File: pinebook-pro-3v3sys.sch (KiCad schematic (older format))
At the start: 19 parts, among them J1 Conn_01x03, J2 Conn_02x03_Counter_Clockwise, J3 Conn_01x01, J4 Conn_01x03, J5 Conn_01x01, U1 TPS63806

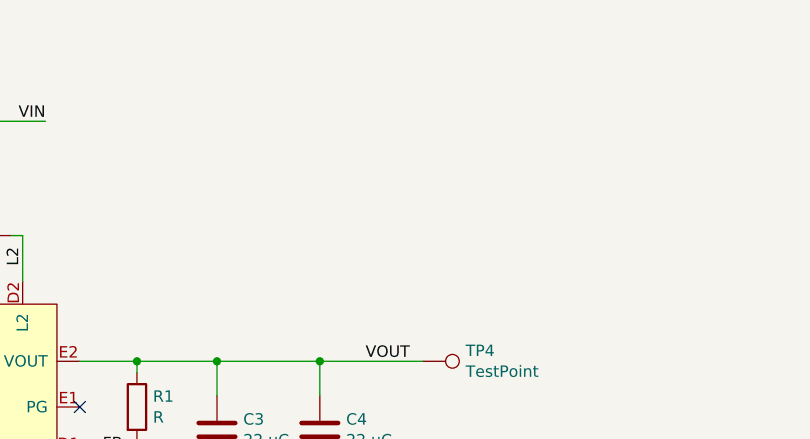
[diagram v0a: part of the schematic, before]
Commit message: Add components for mousebites
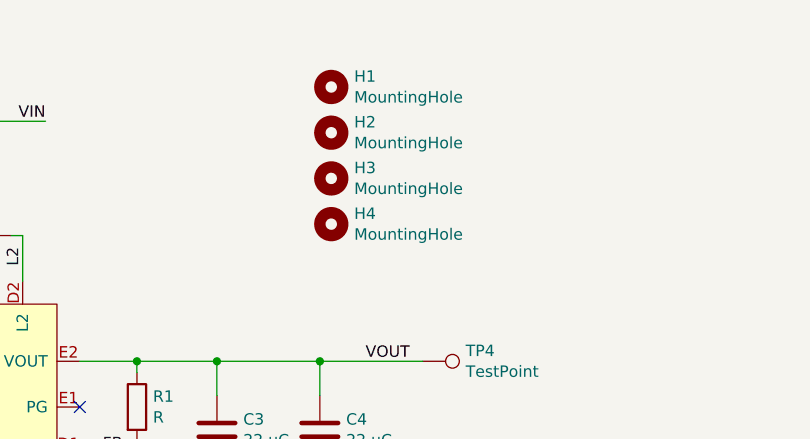
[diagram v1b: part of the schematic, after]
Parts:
- added H1, H2, H3, H4: MountingHole, Mousebite:Mousebite_0.3mm, symbol Mechanical:MountingHole
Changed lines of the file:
@@
 NoConn ~ 9150 3500
 NoConn ~ 9150 3600
+$Comp
+L Mechanical:MountingHole H1
+U 1 1 5DE0908C
+P 6500 1600
+F 0 "H1" H 6600 1646 50  0000 L CNN
+F 1 "MountingHole" H 6600 1555 50  0000 L CNN
+F 2 "Mousebite:Mousebite_0.3mm" H 6500 1600 50  0001 C CNN
+F 3 "~" H 6500 1600 50  0001 C CNN
+	1    6500 1600
+	1    0    0    -1
+$EndComp
+$Comp
+L Mechanical:MountingHole H2
+U 1 1 5DE09669
+P 6500 1800
+F 0 "H2" H 6600 1846 50  0000 L CNN
+F 1 "MountingHole" H 6600 1755 50  0000 L CNN
+F 2 "Mousebite:Mousebite_0.3mm" H 6500 1800 50  0001 C CNN
+F 3 "~" H 6500 1800 50  0001 C CNN
+	1    6500 1800
+	1    0    0    -1
+$EndComp
+$Comp
+L Mechanical:MountingHole H3
+U 1 1 5DE0A1FC
+P 6500 2000
+F 0 "H3" H 6600 2046 50  0000 L CNN
+F 1 "MountingHole" H 6600 1955 50  0000 L CNN
+F 2 "Mousebite:Mousebite_0.3mm" H 6500 2000 50  0001 C CNN
+F 3 "~" H 6500 2000 50  0001 C CNN
+	1    6500 2000
+	1    0    0    -1
+$EndComp
+$Comp
+L Mechanical:MountingHole H4
+U 1 1 5DE0AE24
+P 6500 2200
+F 0 "H4" H 6600 2246 50  0000 L CNN
+F 1 "MountingHole" H 6600 2155 50  0000 L CNN
+F 2 "Mousebite:Mousebite_0.3mm" H 6500 2200 50  0001 C CNN
+F 3 "~" H 6500 2200 50  0001 C CNN
+	1    6500 2200
+	1    0    0    -1
+$EndComp
 $EndSCHEMATC

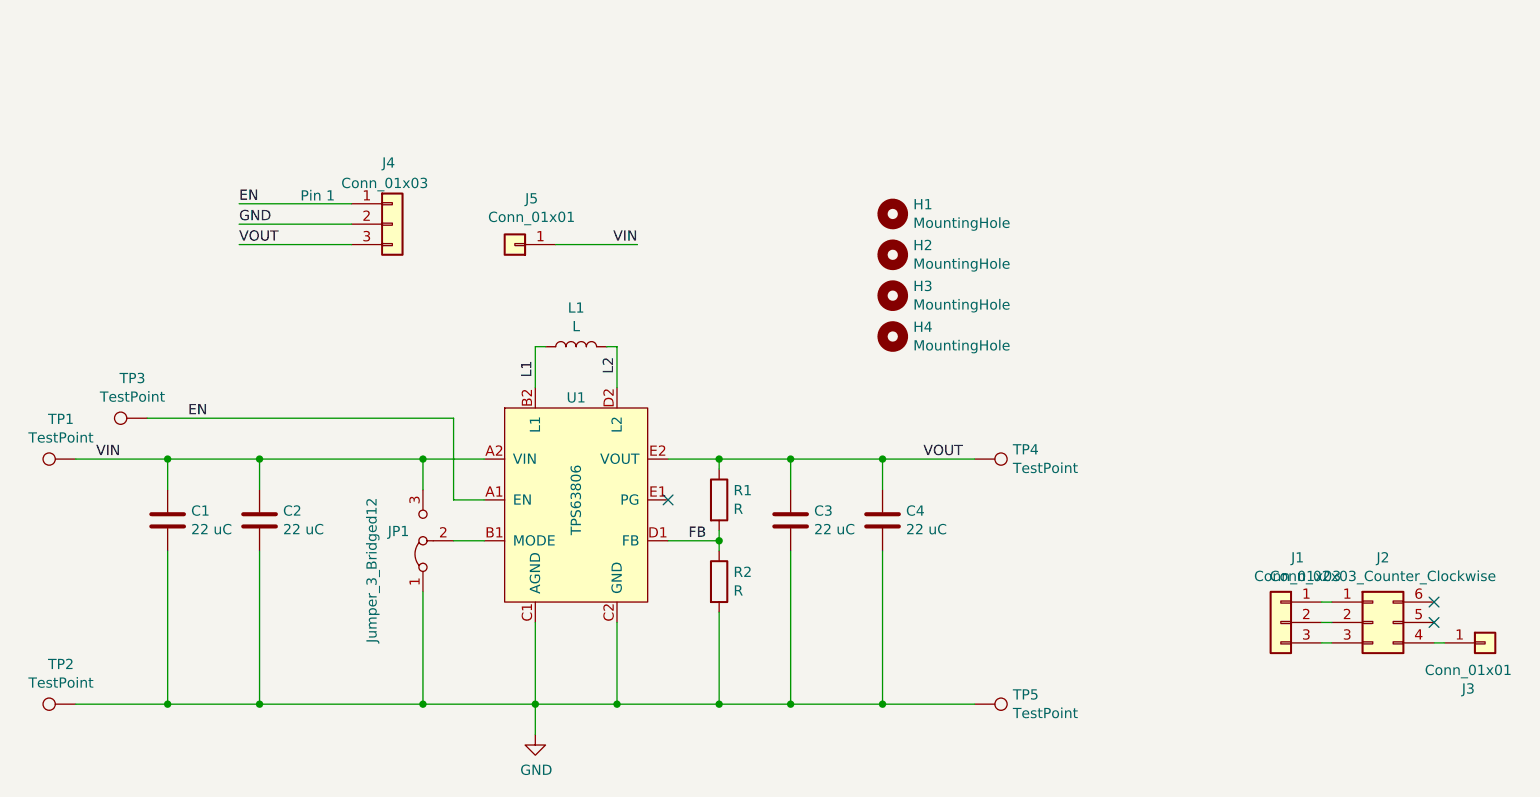
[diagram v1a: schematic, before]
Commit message: Parameterize feedback divider resistors for 3.3 V
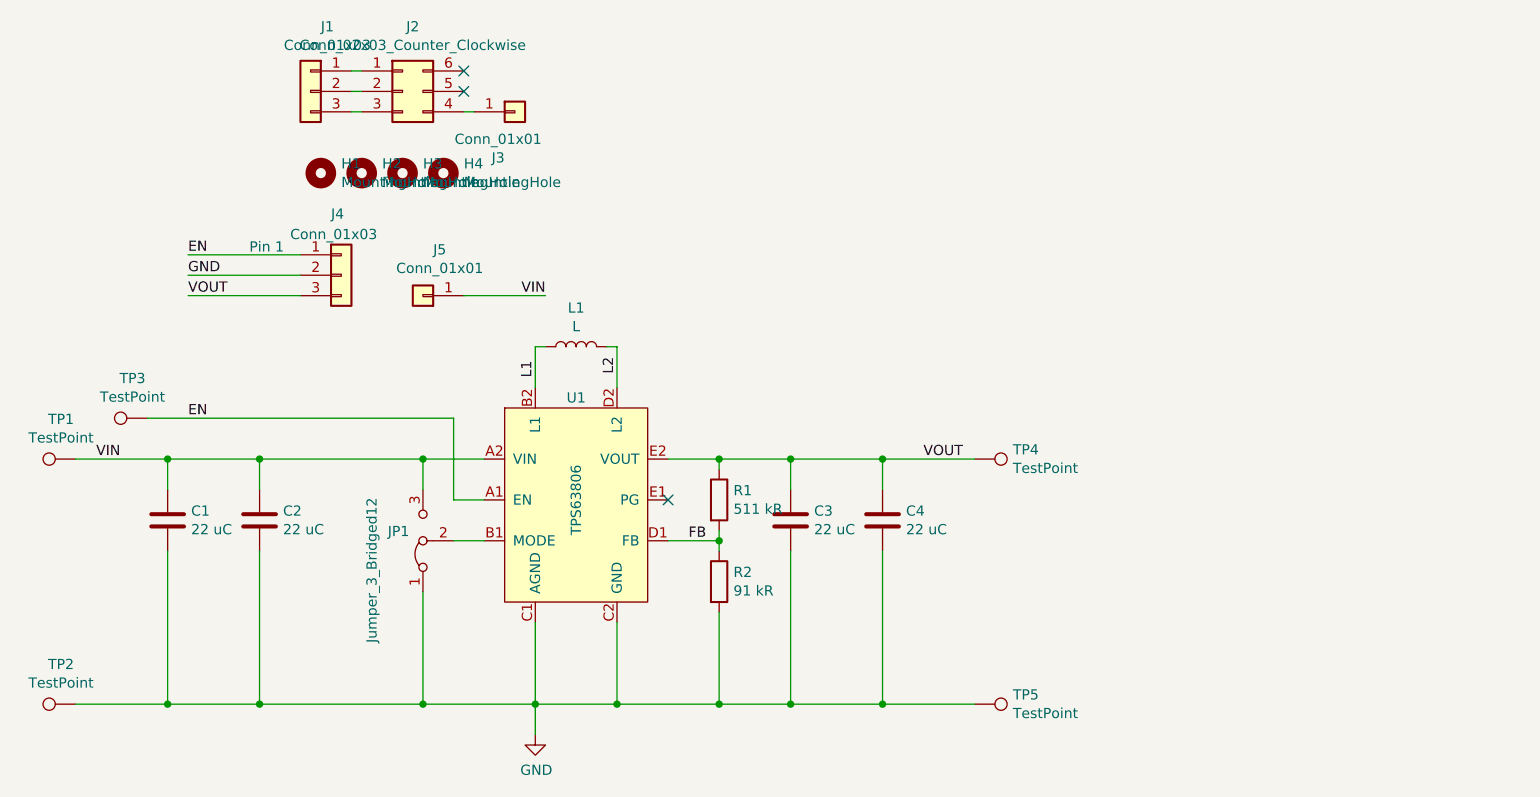
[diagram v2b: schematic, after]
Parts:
- R1: value R -> 511 kR
- R2: value R -> 91 kR
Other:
- moved on the sheet: H1, H2, H3, H4, J1, J2, J3, J4, J5
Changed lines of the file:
@@
 encoding utf-8
 Sheet 1 1
-Title ""
-Date ""
-Rev ""
-Comp ""
+Title "PInebook Pro VCC3V3_SYS regulator board"
+Date "2019-11-24"
+Rev "A"
+Comp "Tobias Schramm"
 Comment1 ""
 Comment2 ""
@@
 P 5650 3000
 F 0 "R1" H 5720 3046 50  0000 L CNN
-F 1 "R" H 5720 2955 50  0000 L CNN
+F 1 "511 kR" H 5720 2955 50  0000 L CNN
 F 2 "Resistor_SMD:R_0402_1005Metric" V 5580 3000 50  0001 C CNN
 F 3 "~" H 5650 3000 50  0001 C CNN
@@
 P 5650 3400
 F 0 "R2" H 5720 3446 50  0000 L CNN
-F 1 "R" H 5720 3355 50  0000 L CNN
+F 1 "91 kR" H 5720 3355 50  0000 L CNN
 F 2 "Resistor_SMD:R_0402_1005Metric" V 5580 3400 50  0001 C CNN
 F 3 "~" H 5650 3400 50  0001 C CNN
@@
 L Connector_Generic:Conn_02x03_Counter_Clockwise J2
 U 1 1 5DDB932F
-P 8850 3600
-F 0 "J2" H 8900 3917 50  0000 C CNN
-F 1 "Conn_02x03_Counter_Clockwise" H 8900 3826 50  0000 C CNN
-F 2 "Castellations:SOT-23-6" H 8850 3600 50  0001 C CNN
-F 3 "~" H 8850 3600 50  0001 C CNN
-	1    8850 3600
+P 4100 1000
+F 0 "J2" H 4150 1317 50  0000 C CNN
+F 1 "Conn_02x03_Counter_Clockwise" H 4150 1226 50  0000 C CNN
+F 2 "Castellations:SOT-23-6" H 4100 1000 50  0001 C CNN
+F 3 "~" H 4100 1000 50  0001 C CNN
+	1    4100 1000
 	1    0    0    -1
 $EndComp
@@
 L Connector_Generic:Conn_01x03 J1
 U 1 1 5DDBA462
-P 8400 3600
-F 0 "J1" H 8318 3917 50  0000 C CNN
-F 1 "Conn_01x03" H 8318 3826 50  0000 C CNN
-F 2 "Connector_PinHeader_0.6mm:PinHeader_1x03_P0.95mm" H 8400 3600 50  0001 C CNN
-F 3 "~" H 8400 3600 50  0001 C CNN
-	1    8400 3600
+P 3650 1000
+F 0 "J1" H 3568 1317 50  0000 C CNN
+F 1 "Conn_01x03" H 3568 1226 50  0000 C CNN
+F 2 "Connector_PinHeader_0.6mm:PinHeader_1x03_P0.95mm" H 3650 1000 50  0001 C CNN
+F 3 "~" H 3650 1000 50  0001 C CNN
+	1    3650 1000
 	-1   0    0    -1
 $EndComp
 Wire Wire Line
-	8600 3500 8650 3500
-Wire Wire Line
-	8600 3600 8650 3600
-Wire Wire Line
-	8600 3700 8650 3700
+	3850 900  3900 900
+Wire Wire Line
+	3850 1000 3900 1000
+Wire Wire Line
+	3850 1100 3900 1100
 Text Label 4750 2400 1    50   ~ 0
 L1
@@
 L Connector_Generic:Conn_01x03 J4
 U 1 1 5DDD7088
-P 4050 1650
-F 0 "J4" H 4000 1950 50  0000 L CNN
-F 1 "Conn_01x03" H 3800 1850 50  0000 L CNN
-F 2 "Connector_PinHeader_0.6mm:PinHeader_1x03_P0.95mm" H 4050 1650 50  0001 C CNN
-F 3 "~" H 4050 1650 50  0001 C CNN
-	1    4050 1650
-	1    0    0    -1
-$EndComp
-Text Notes 3600 1550 0    50   ~ 0
+P 3800 1900
+F 0 "J4" H 3750 2200 50  0000 L CNN
+F 1 "Conn_01x03" H 3550 2100 50  0000 L CNN
+F 2 "Connector_PinHeader_0.6mm:PinHeader_1x03_P0.95mm" H 3800 1900 50  0001 C CNN
+F 3 "~" H 3800 1900 50  0001 C CNN
+	1    3800 1900
+	1    0    0    -1
+$EndComp
+Text Notes 3350 1800 0    50   ~ 0
 Pin 1\n
 Wire Wire Line
-	3850 1550 3300 1550
-Text Label 3300 1550 0    50   ~ 0
+	3600 1800 3050 1800
+Text Label 3050 1800 0    50   ~ 0
 EN
 Wire Wire Line
-	3850 1650 3300 1650
-Text Label 3300 1650 0    50   ~ 0
+	3600 1900 3050 1900
+Text Label 3050 1900 0    50   ~ 0
 GND
 Wire Wire Line
-	3850 1750 3300 1750
-Text Label 3300 1750 0    50   ~ 0
+	3600 2000 3050 2000
+Text Label 3050 2000 0    50   ~ 0
 VOUT
 Wire Wire Line
-	4850 1750 5250 1750
-Text Label 5250 1750 2    50   ~ 0
+	4400 2000 4800 2000
+Text Label 4800 2000 2    50   ~ 0
 VIN
 $Comp
@@
 L Connector_Generic:Conn_01x01 J5
 U 1 1 5DDE7032
-P 4650 1750
-F 0 "J5" H 4568 1525 50  0000 C CNN
-F 1 "Conn_01x01" H 4568 1616 50  0000 C CNN
-F 2 "Connector_PinHeader_0.6mm:PinHeader_1x01_P0.95mm" H 4650 1750 50  0001 C CNN
-F 3 "~" H 4650 1750 50  0001 C CNN
-	1    4650 1750
+P 4200 2000
+F 0 "J5" H 4118 1775 50  0000 C CNN
+F 1 "Conn_01x01" H 4118 1866 50  0000 C CNN
+F 2 "Connector_PinHeader_0.6mm:PinHeader_1x01_P0.95mm" H 4200 2000 50  0001 C CNN
+F 3 "~" H 4200 2000 50  0001 C CNN
+	1    4200 2000
 	-1   0    0    1
 $EndComp
@@
 L Connector_Generic:Conn_01x01 J3
 U 1 1 5DDFD1C1
-P 9400 3700
-F 0 "J3" H 9318 3475 50  0000 C CNN
-F 1 "Conn_01x01" H 9318 3566 50  0000 C CNN
-F 2 "Connector_PinHeader_0.6mm:PinHeader_1x01_P0.95mm" H 9400 3700 50  0001 C CNN
-F 3 "~" H 9400 3700 50  0001 C CNN
-	1    9400 3700
-	1    0    0    -1
-$EndComp
-Wire Wire Line
-	9200 3700 9150 3700
-NoConn ~ 9150 3500
-NoConn ~ 9150 3600
+P 4650 1100
+F 0 "J3" H 4568 875 50  0000 C CNN
+F 1 "Conn_01x01" H 4568 966 50  0000 C CNN
+F 2 "Connector_PinHeader_0.6mm:PinHeader_1x01_P0.95mm" H 4650 1100 50  0001 C CNN
+F 3 "~" H 4650 1100 50  0001 C CNN
+	1    4650 1100
+	1    0    0    -1
+$EndComp
+Wire Wire Line
+	4450 1100 4400 1100
+NoConn ~ 4400 900
+NoConn ~ 4400 1000
 $Comp
 L Mechanical:MountingHole H1
 U 1 1 5DE0908C
-P 6500 1600
-F 0 "H1" H 6600 1646 50  0000 L CNN
-F 1 "MountingHole" H 6600 1555 50  0000 L CNN
-F 2 "Mousebite:Mousebite_0.3mm" H 6500 1600 50  0001 C CNN
-F 3 "~" H 6500 1600 50  0001 C CNN
-	1    6500 1600
+P 3700 1400
+F 0 "H1" H 3800 1446 50  0000 L CNN
+F 1 "MountingHole" H 3800 1355 50  0000 L CNN
+F 2 "Mousebite:Mousebite_0.3mm" H 3700 1400 50  0001 C CNN
+F 3 "~" H 3700 1400 50  0001 C CNN
+	1    3700 1400
 	1    0    0    -1
 $EndComp
@@
 L Mechanical:MountingHole H2
 U 1 1 5DE09669
-P 6500 1800
-F 0 "H2" H 6600 1846 50  0000 L CNN
-F 1 "MountingHole" H 6600 1755 50  0000 L CNN
-F 2 "Mousebite:Mousebite_0.3mm" H 6500 1800 50  0001 C CNN
-F 3 "~" H 6500 1800 50  0001 C CNN
-	1    6500 1800
+P 3900 1400
+F 0 "H2" H 4000 1446 50  0000 L CNN
+F 1 "MountingHole" H 4000 1355 50  0000 L CNN
+F 2 "Mousebite:Mousebite_0.3mm" H 3900 1400 50  0001 C CNN
+F 3 "~" H 3900 1400 50  0001 C CNN
+	1    3900 1400
 	1    0    0    -1
 $EndComp
@@
 L Mechanical:MountingHole H3
 U 1 1 5DE0A1FC
-P 6500 2000
-F 0 "H3" H 6600 2046 50  0000 L CNN
-F 1 "MountingHole" H 6600 1955 50  0000 L CNN
-F 2 "Mousebite:Mousebite_0.3mm" H 6500 2000 50  0001 C CNN
-F 3 "~" H 6500 2000 50  0001 C CNN
-	1    6500 2000
+P 4100 1400
+F 0 "H3" H 4200 1446 50  0000 L CNN
+F 1 "MountingHole" H 4200 1355 50  0000 L CNN
+F 2 "Mousebite:Mousebite_0.3mm" H 4100 1400 50  0001 C CNN
+F 3 "~" H 4100 1400 50  0001 C CNN
+	1    4100 1400
 	1    0    0    -1
 $EndComp
@@
 L Mechanical:MountingHole H4
 U 1 1 5DE0AE24
-P 6500 2200
-F 0 "H4" H 6600 2246 50  0000 L CNN
-F 1 "MountingHole" H 6600 2155 50  0000 L CNN
-F 2 "Mousebite:Mousebite_0.3mm" H 6500 2200 50  0001 C CNN
-F 3 "~" H 6500 2200 50  0001 C CNN
-	1    6500 2200
-	1    0    0    -1
-$EndComp
+P 4300 1400
+F 0 "H4" H 4400 1446 50  0000 L CNN
+F 1 "MountingHole" H 4400 1355 50  0000 L CNN
+F 2 "Mousebite:Mousebite_0.3mm" H 4300 1400 50  0001 C CNN
+F 3 "~" H 4300 1400 50  0001 C CNN
+	1    4300 1400
+	1    0    0    -1
+$EndComp
